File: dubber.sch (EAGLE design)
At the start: 31 parts, among them IC1 LM324N, P1-G TPSQPAD1-13Y, P1-S TPSQPAD1-13Y, P2-G TPSQPAD1-13Y, P2-S TPSQPAD1-13Y, P3-G TPSQPAD1-13Y, P3-S TPSQPAD1-13Y

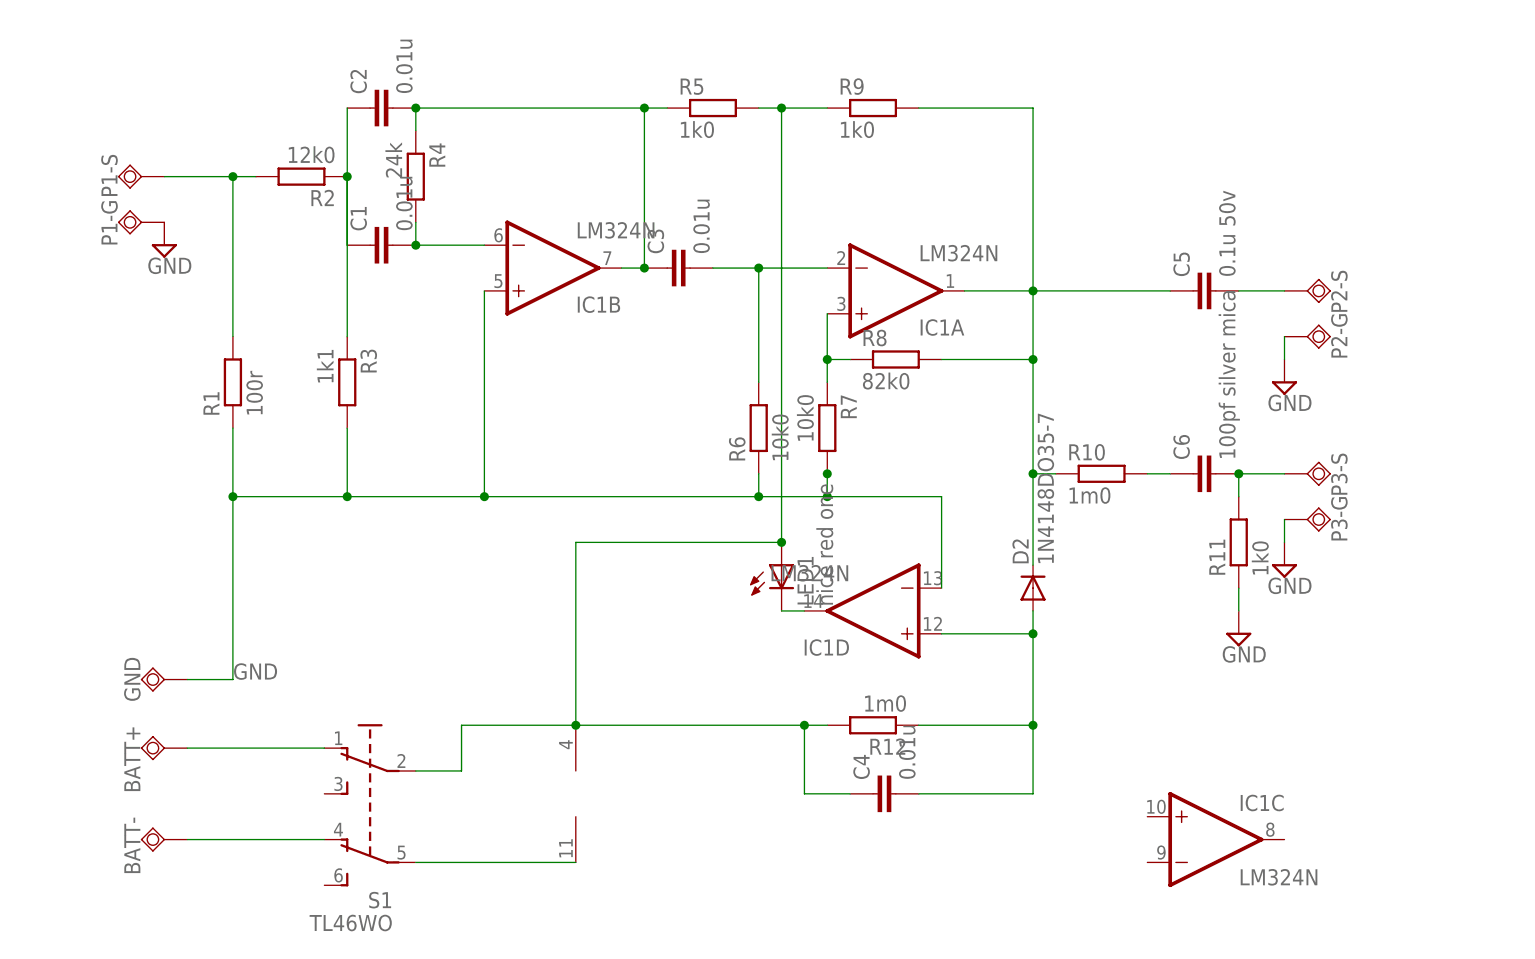
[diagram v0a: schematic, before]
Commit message: ocd round 2, schematic cleanup and moving components into space
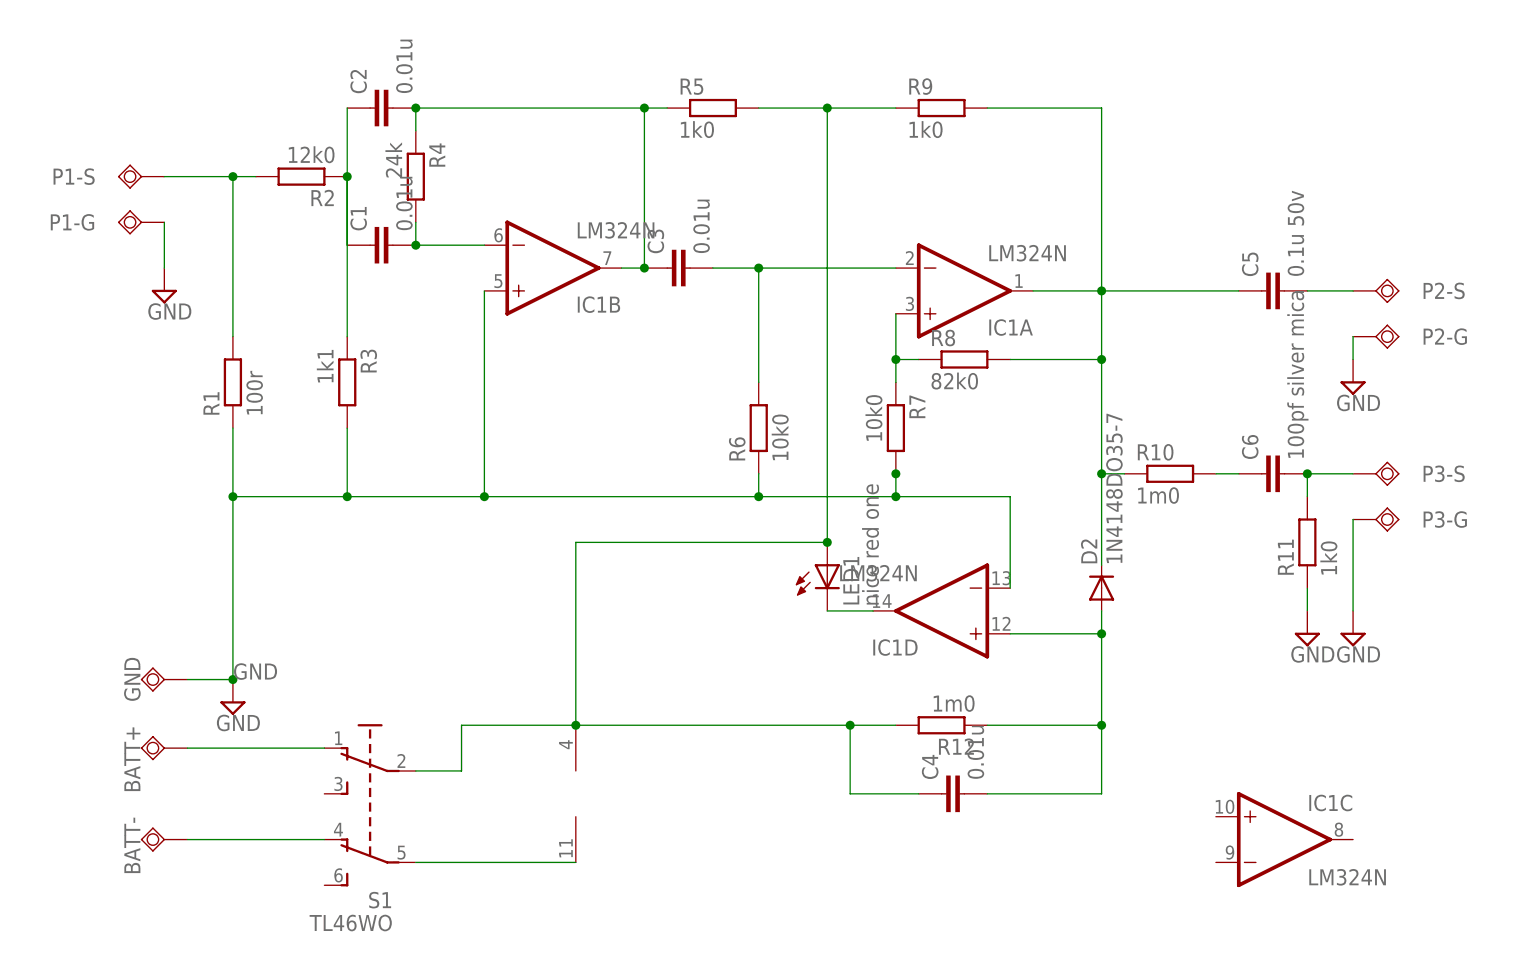
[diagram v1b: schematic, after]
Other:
- moved on the sheet: C4, C5, C6, D2, IC1A, IC1C, IC1D, LED1, P2-G, P2-S, P3-G, P3-S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

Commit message: tweaks again
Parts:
- renumbered BATT+ to +, BATT- to -, P1-S to INPUT, P2-S to OUTPUT, P3-S to SLAVE
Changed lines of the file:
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@@
 <?xml version="1.0" encoding="utf-8"?>
 <!DOCTYPE eagle SYSTEM "eagle.dtd">
-<eagle version="7.3.0">
+<eagle version="7.6.0">
 <drawing>
 <settings>
@@
 <part name="D2" library="diode" deviceset="1N4148" device="DO35-7"/>
 <part name="LED1" library="led" deviceset="LED" device="5MM" value="nice red one"/>
-<part name="P1-S" library="testpad" deviceset="TPSQ" device="PAD1-13Y"/>
+<part name="INPUT" library="testpad" deviceset="TPSQ" device="PAD1-13Y"/>
 <part name="P1-G" library="testpad" deviceset="TPSQ" device="PAD1-13Y"/>
-<part name="P2-S" library="testpad" deviceset="TPSQ" device="PAD1-13Y"/>
+<part name="OUTPUT" library="testpad" deviceset="TPSQ" device="PAD1-13Y"/>
 <part name="P2-G" library="testpad" deviceset="TPSQ" device="PAD1-13Y"/>
-<part name="P3-S" library="testpad" deviceset="TPSQ" device="PAD1-13Y"/>
+<part name="SLAVE" library="testpad" deviceset="TPSQ" device="PAD1-13Y"/>
 <part name="P3-G" library="testpad" deviceset="TPSQ" device="PAD1-13Y"/>
-<part name="BATT+" library="testpad" deviceset="TPSQ" device="PAD1-13Y"/>
+<part name="+" library="testpad" deviceset="TPSQ" device="PAD1-13Y"/>
 <part name="GND" library="testpad" deviceset="TPSQ" device="PAD1-13Y"/>
-<part name="BATT-" library="testpad" deviceset="TPSQ" device="PAD1-13Y"/>
+<part name="-" library="testpad" deviceset="TPSQ" device="PAD1-13Y"/>
 <part name="SUPPLY1" library="supply2" deviceset="GND" device=""/>
 <part name="SUPPLY2" library="supply2" deviceset="GND" device=""/>
@@
 <instance part="D2" gate="G$1" x="116.84" y="35.56" rot="R90"/>
 <instance part="LED1" gate="G$1" x="86.36" y="38.1"/>
-<instance part="P1-S" gate="G$1" x="10.16" y="81.28" smashed="yes" rot="R270">
+<instance part="INPUT" gate="G$1" x="10.16" y="81.28" smashed="yes" rot="R270">
 <attribute name="NAME" x="5.08" y="81.28" size="1.778" layer="95" rot="R180" align="center-left"/>
 <attribute name="TP_SIGNAL_NAME" x="8.89" y="78.74" size="1.778" layer="97" rot="R270"/>
 </instance>
 <instance part="P1-G" gate="G$1" x="10.16" y="76.2" smashed="yes" rot="R270">
-<attribute name="NAME" x="5.08" y="76.2" size="1.778" layer="95" rot="R180" align="center-left"/>
 <attribute name="TP_SIGNAL_NAME" x="8.89" y="73.66" size="1.778" layer="97" rot="R270"/>
 </instance>
-<instance part="P2-S" gate="G$1" x="147.32" y="68.58" smashed="yes" rot="R90">
+<instance part="OUTPUT" gate="G$1" x="147.32" y="68.58" smashed="yes" rot="R90">
 <attribute name="NAME" x="152.4" y="68.58" size="1.778" layer="95" align="center-left"/>
 <attribute name="TP_SIGNAL_NAME" x="148.59" y="71.12" size="1.778" layer="97" rot="R90"/>
 </instance>
 <instance part="P2-G" gate="G$1" x="147.32" y="63.5" smashed="yes" rot="R90">
-<attribute name="NAME" x="152.4" y="63.5" size="1.778" layer="95" align="center-left"/>
 <attribute name="TP_SIGNAL_NAME" x="148.59" y="66.04" size="1.778" layer="97" rot="R90"/>
 </instance>
-<instance part="P3-S" gate="G$1" x="147.32" y="48.26" smashed="yes" rot="R90">
+<instance part="SLAVE" gate="G$1" x="147.32" y="48.26" smashed="yes" rot="R90">
 <attribute name="NAME" x="152.4" y="48.26" size="1.778" layer="95" align="center-left"/>
 <attribute name="TP_SIGNAL_NAME" x="148.59" y="50.8" size="1.778" layer="97" rot="R90"/>
 </instance>
 <instance part="P3-G" gate="G$1" x="147.32" y="43.18" smashed="yes" rot="R90">
-<attribute name="NAME" x="152.4" y="43.18" size="1.778" layer="95" align="center-left"/>
 <attribute name="TP_SIGNAL_NAME" x="148.59" y="45.72" size="1.778" layer="97" rot="R90"/>
 </instance>
-<instance part="BATT+" gate="G$1" x="12.7" y="17.78" rot="R270"/>
+<instance part="+" gate="G$1" x="12.7" y="17.78" rot="R270"/>
 <instance part="GND" gate="G$1" x="12.7" y="25.4" rot="R270"/>
-<instance part="BATT-" gate="G$1" x="12.7" y="7.62" rot="R270"/>
+<instance part="-" gate="G$1" x="12.7" y="7.62" rot="R270"/>
 <instance part="SUPPLY1" gate="GND" x="12.7" y="68.58"/>
 <instance part="SUPPLY2" gate="GND" x="144.78" y="58.42"/>
@@
 <net name="N$4" class="0">
 <segment>
-<pinref part="BATT+" gate="G$1" pin="TP"/>
+<pinref part="+" gate="G$1" pin="TP"/>
 <wire x1="15.24" y1="17.78" x2="30.48" y2="17.78" width="0.1524" layer="91"/>
 <pinref part="S1" gate="BEF1" pin="O"/>
@@
 <net name="N$5" class="0">
 <segment>
-<pinref part="BATT-" gate="G$1" pin="TP"/>
+<pinref part="-" gate="G$1" pin="TP"/>
 <wire x1="15.24" y1="7.62" x2="30.48" y2="7.62" width="0.1524" layer="91"/>
 <pinref part="S1" gate="BEF1" pin="O1"/>
@@
 <net name="N$14" class="0">
 <segment>
-<pinref part="P2-S" gate="G$1" pin="TP"/>
+<pinref part="OUTPUT" gate="G$1" pin="TP"/>
 <pinref part="C5" gate="G$1" pin="2"/>
 <wire x1="144.78" y1="68.58" x2="139.7" y2="68.58" width="0.1524" layer="91"/>
@@
 <net name="N$17" class="0">
 <segment>
-<pinref part="P1-S" gate="G$1" pin="TP"/>
+<pinref part="INPUT" gate="G$1" pin="TP"/>
 <wire x1="12.7" y1="81.28" x2="20.32" y2="81.28" width="0.1524" layer="91"/>
 <pinref part="R2" gate="G$1" pin="2"/>
@@
 <pinref part="C6" gate="G$1" pin="2"/>
 <wire x1="139.7" y1="45.72" x2="139.7" y2="48.26" width="0.1524" layer="91"/>
-<pinref part="P3-S" gate="G$1" pin="TP"/>
+<pinref part="SLAVE" gate="G$1" pin="TP"/>
 <wire x1="139.7" y1="48.26" x2="144.78" y2="48.26" width="0.1524" layer="91"/>
 <junction x="139.7" y="48.26"/>
